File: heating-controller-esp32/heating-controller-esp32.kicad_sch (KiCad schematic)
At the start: 11 parts, among them J10 76829-0104, J4 76829-0104, J5 76829-0104, J6 76829-0104, J7 76829-0104, J8 76829-0104, J9 76829-0104

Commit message: Initial design of schematic complete. Started laying out PCB
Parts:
- added Brd1: SSD1306, Andrew_Custom:128x64OLED, symbol SSD1306-128x64_OLED:SSD1306
- added JP1, JP4: i2cPU, Jumper:SolderJumper-2_P1.3mm_Bridged_RoundedPad1.0x1.5mm, symbol Jumper:SolderJumper_2_Bridged
- added R42, R43: 10K, Resistor_SMD:R_0603_1608Metric, symbol Device:R
- added TP1, TP2: TestPoint, TestPoint:TestPoint_Keystone_5005-5009_Compact, symbol Connector:TestPoint
- gave numbers to parts that had none: 1
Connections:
- net +3V3: now also Brd1.2 (VCC)
- net ESP32/IO32: now also Brd1.4 (SDA), JP1.2 (B), TP2.1
- net ESP32/IO33: now also Brd1.3 (SCL), JP4.2 (B), TP1.1
- net GND: now also Brd1.1 (GND)
- new net: JP1.1 (A), R42.1
- new net: JP4.1 (A), R43.1
- new net 3.3V: R42.2, R43.2
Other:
- moved on the sheet: J4

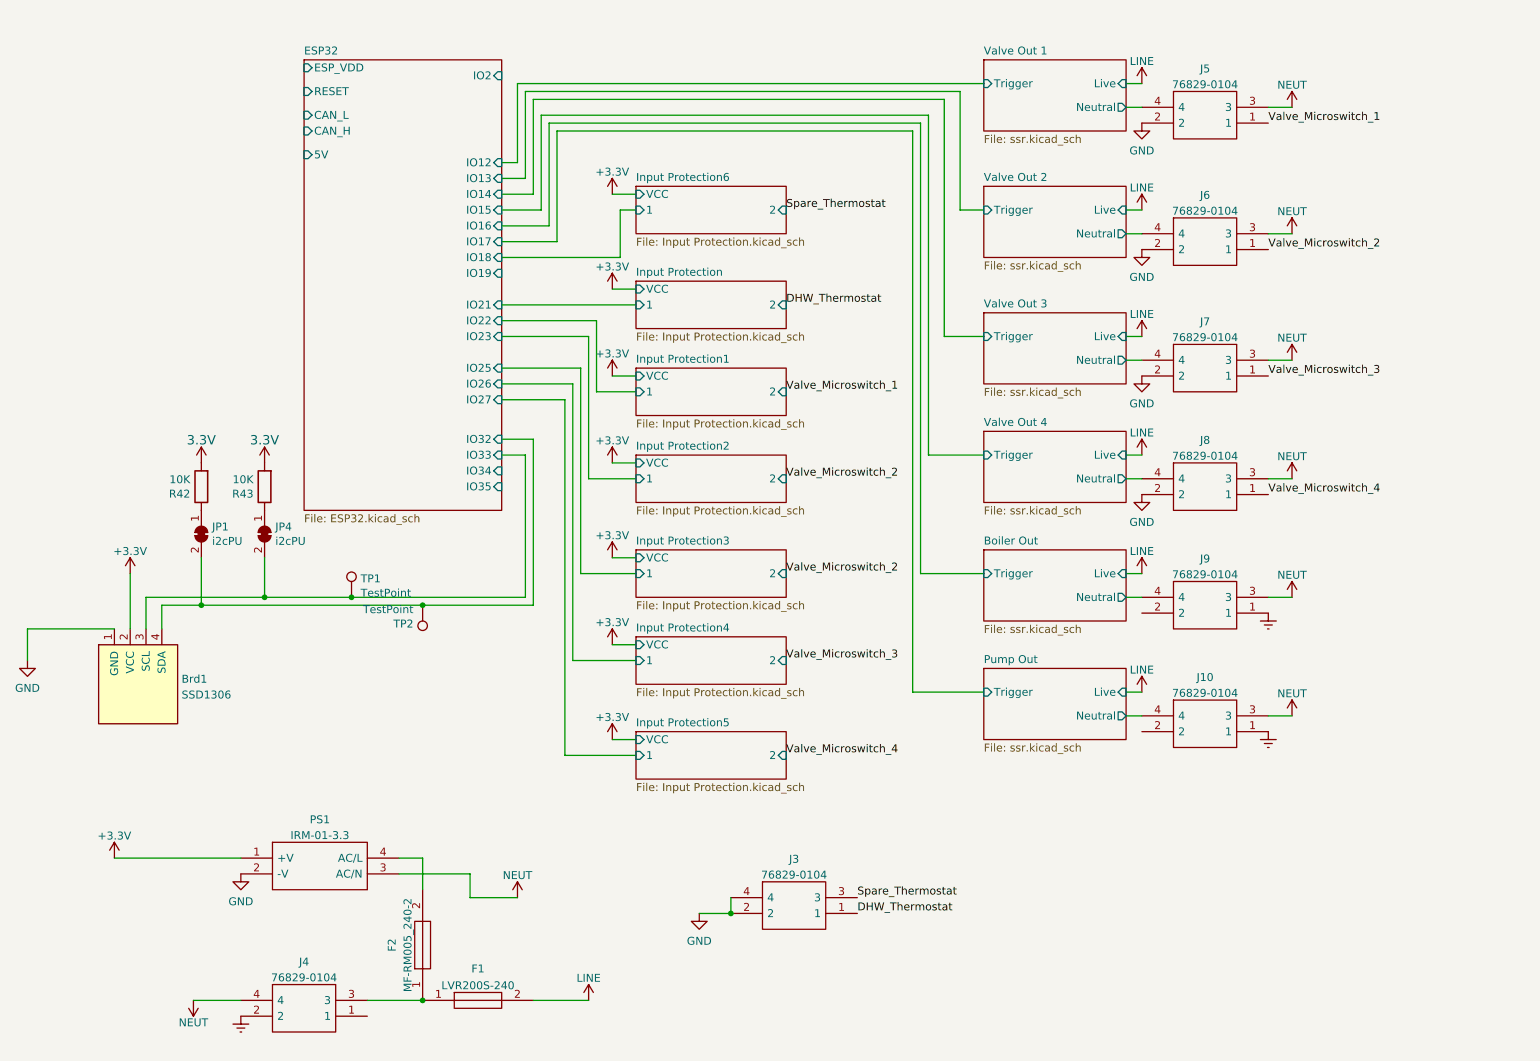
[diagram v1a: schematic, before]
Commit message: Changed to Wago connectors; initial routing completed
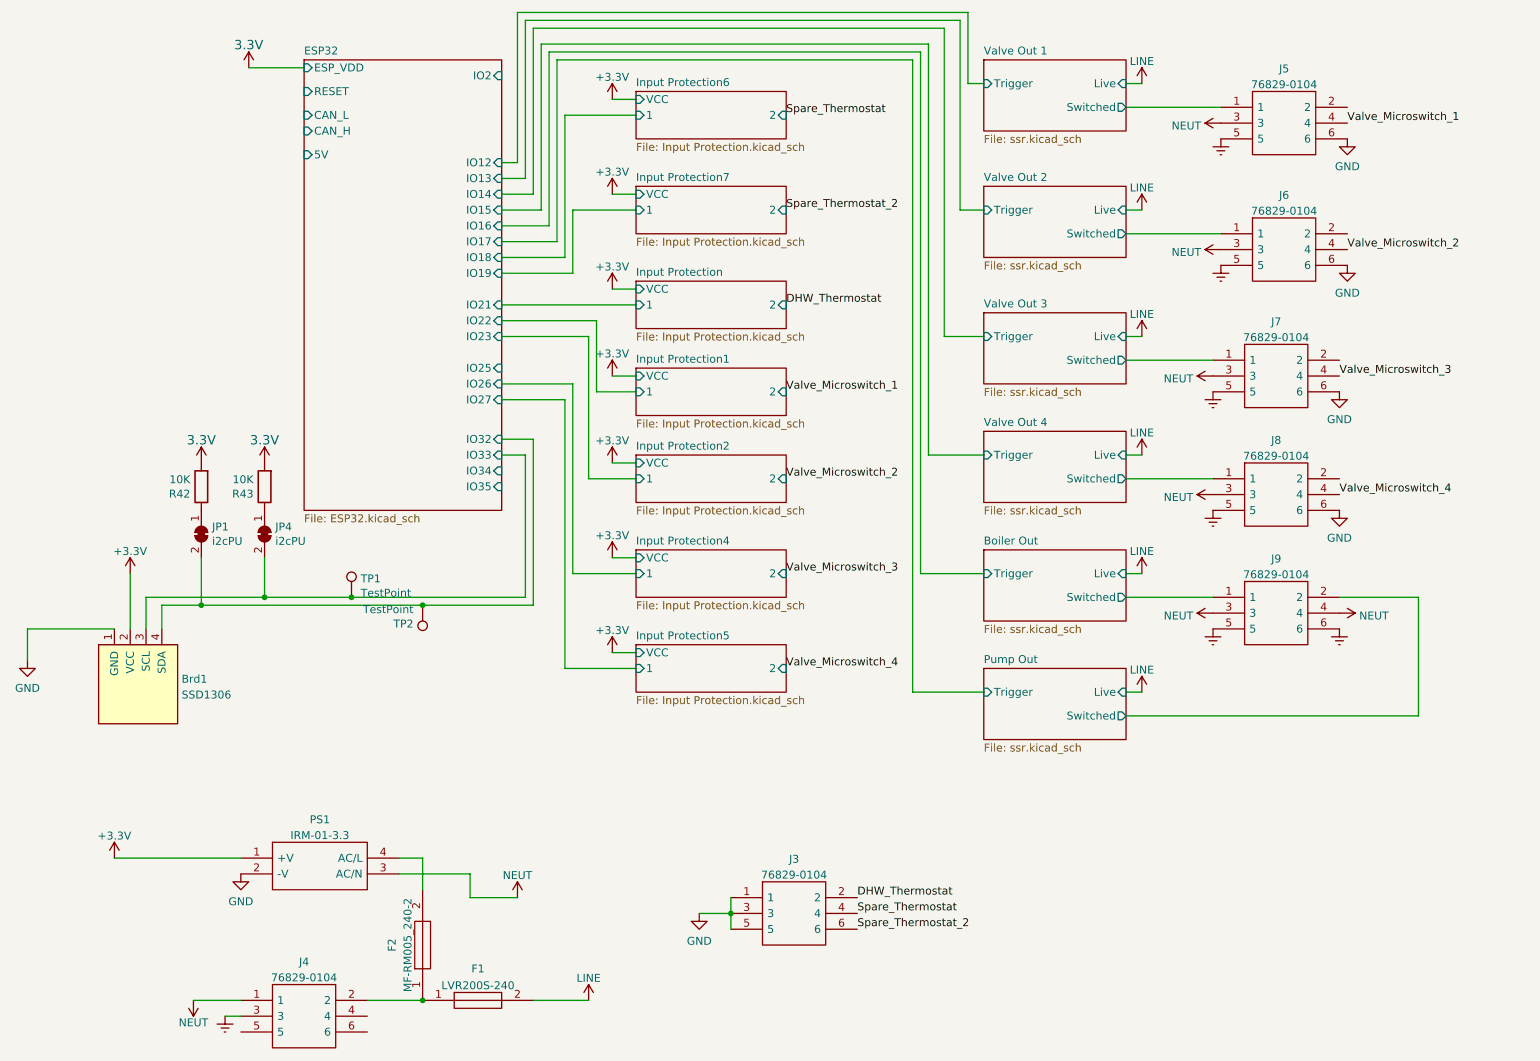
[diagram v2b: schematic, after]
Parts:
- removed J10: 76829-0104, SamacSys_Parts:768290104, symbol SamacSys_Parts:76829-0104
- J3, J4, J5, J6, J7, J8, J9: footprint SamacSys_Parts:768290104 -> 736303; symbol SamacSys_Parts:76829-0104 -> SamacSys_Parts:736-303; Height 14 -> 26.5; Manufacturer_Name Molex -> Wago; Manufacturer_Part_Number 76829-0104 -> 736-303
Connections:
- net 3.3V is gone; now on net +3V3: R42.2, R43.2
- net Boiler Out/Neutral is gone; now on net NEUT: J9.4
- net Valve Out 1/Neutral is gone; now on net Valve_Microswitch_1: J5.4
- net Valve Out 2/Neutral is gone; now on net Valve_Microswitch_2: J6.4
- net Valve Out 3/Neutral is gone; now on net Valve_Microswitch_3: J7.4
- net Valve Out 4/Neutral is gone; now on net Valve_Microswitch_4: J8.4
- net DHW_Thermostat: now also J3.2; no longer J3.1
- net Earth: now also J4.3, J5.5, J6.5, J7.5, J8.5, J9.5, J9.6; no longer J4.2, J9.1
- net GND: now also J3.1, J3.3, J3.5, J5.6, J6.6, J7.6, J8.6; no longer J3.2, J3.4, J5.2, J6.2, J7.2, J8.2
- net NEUT: now also J4.1; no longer J4.4
- net Spare_Thermostat: now also J3.4; no longer J3.3
- net Valve_Microswitch_1: no longer J5.1
- net Valve_Microswitch_2: no longer J6.1
- net Valve_Microswitch_3: no longer J7.1
- net Valve_Microswitch_4: no longer J8.1
- net at F1.1, F2.1: now also J4.2; no longer J4.3
- net Pump Out/Switched: now reaches J9.2
- new net Boiler Out/Switched: J9.1
- new net Spare_Thermostat_2: J3.6
- new net Valve Out 1/Switched: J5.1
- new net Valve Out 2/Switched: J6.1
- new net Valve Out 3/Switched: J7.1
- new net Valve Out 4/Switched: J8.1
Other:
- removed sheet Input Protection3
- added sheet Input Protection7 (Input Protection.kicad_sch)
- sheet Boiler Out ports: added Switched; removed Neutral
- sheet Pump Out ports: added Switched; removed Neutral
- sheet Valve Out 1 ports: added Switched; removed Neutral
- sheet Valve Out 2 ports: added Switched; removed Neutral
- sheet Valve Out 3 ports: added Switched; removed Neutral
- sheet Valve Out 4 ports: added Switched; removed Neutral

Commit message: Added additional spare thermostat inputs
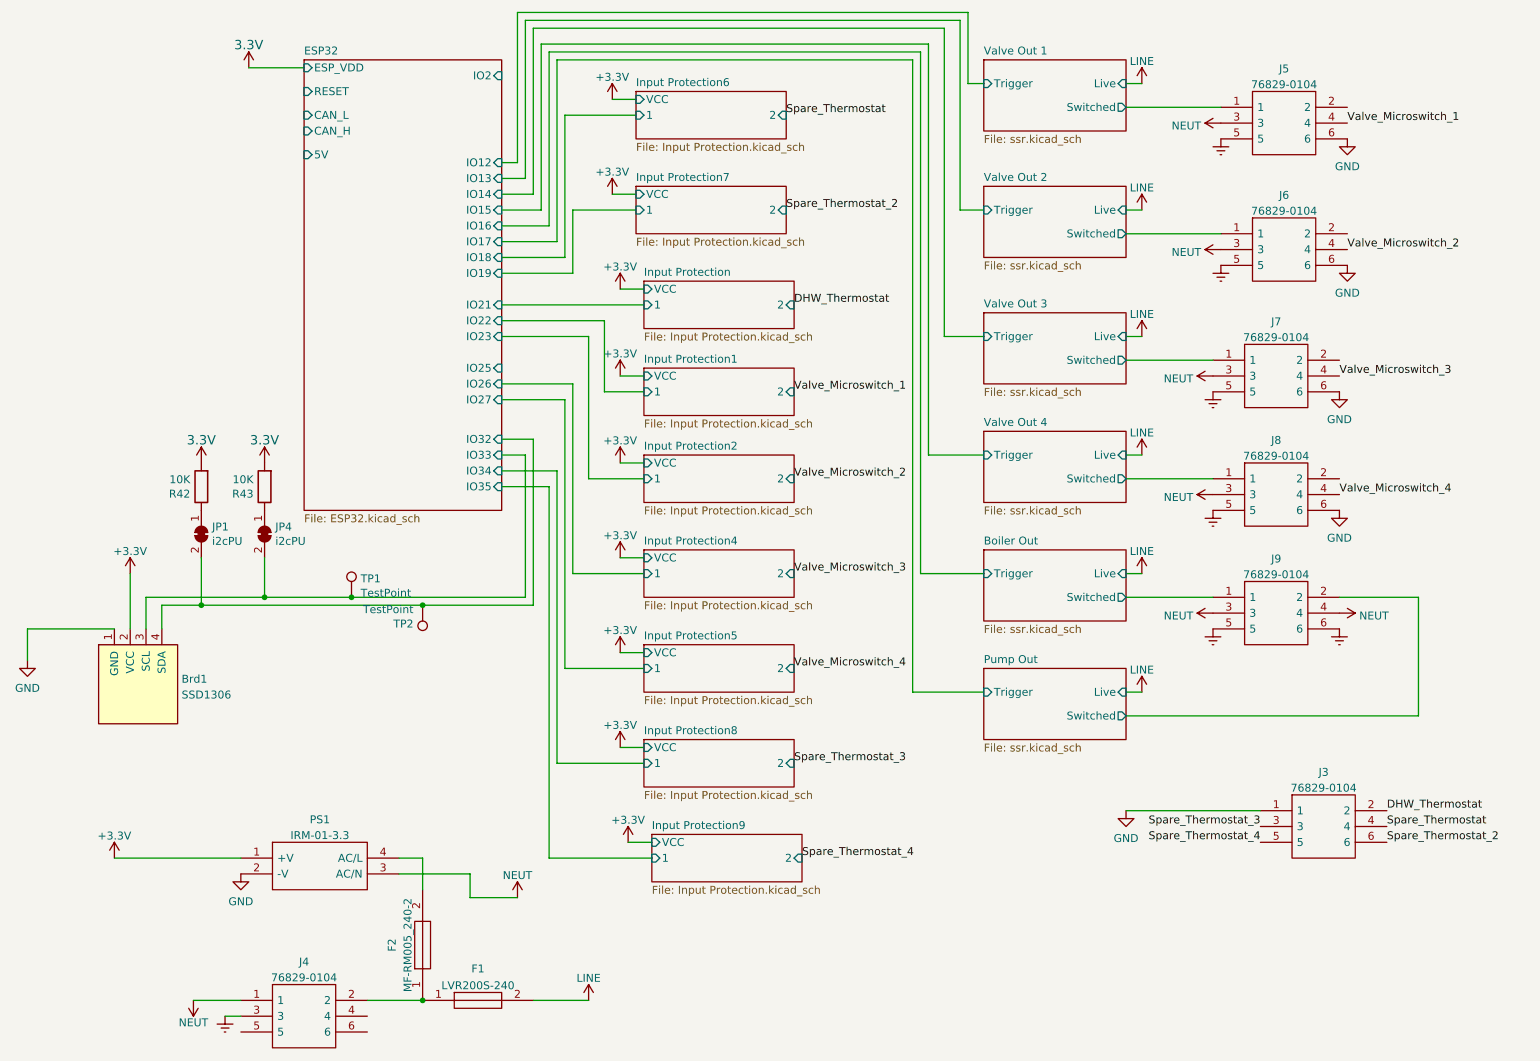
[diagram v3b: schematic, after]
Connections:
- net GND: no longer J3.3, J3.5
- new net Spare_Thermostat_3: J3.3
- new net Spare_Thermostat_4: J3.5
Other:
- added sheet Input Protection8 (Input Protection.kicad_sch)
- added sheet Input Protection9 (Input Protection.kicad_sch)
- moved on the sheet: J3

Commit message: Mounting holes, a few more tweaks
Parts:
- added H? (x4): MountingHole, MountingHole:MountingHole_3.2mm_M3_DIN965, symbol Mechanical:MountingHole

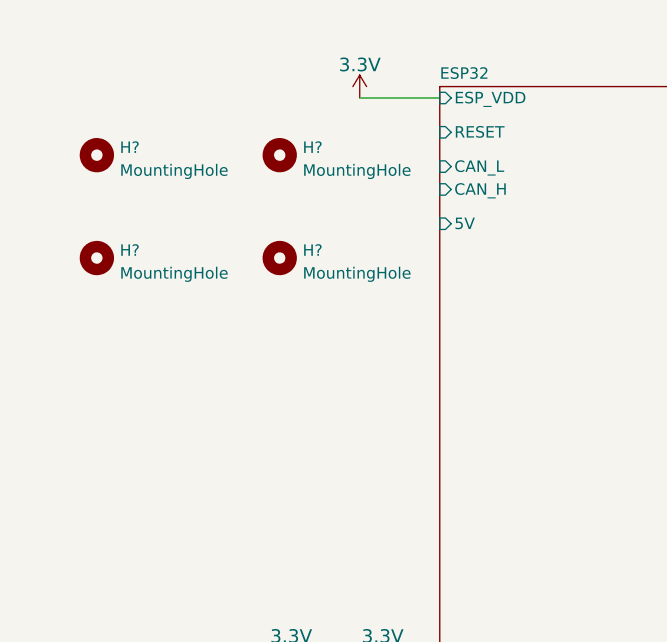
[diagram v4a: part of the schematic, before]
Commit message: Oops. Missing certain files for commit.
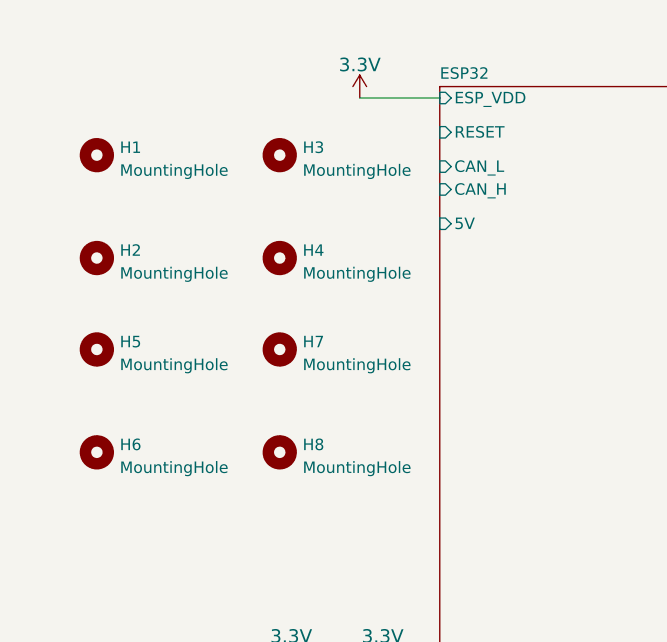
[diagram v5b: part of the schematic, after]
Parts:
- added H5, H6, H7, H8: MountingHole, MountingHole:MountingHole_3.2mm_M3_DIN965, symbol Mechanical:MountingHole
- J3, J4, J5, J6, J7, J8, J9: footprint 736303 -> SamacSys_Parts:736303
- gave numbers to parts that had none: 4
